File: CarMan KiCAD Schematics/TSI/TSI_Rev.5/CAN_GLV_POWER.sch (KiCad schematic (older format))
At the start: 40 parts, among them J30 J23, K2 G5LE-1-E, K3 SFS2-DC24V, K4 SFS2-DC24V, Q11 TN2130K1-G, U14 Bottom Left, U15 Top Left, U17 Top Right, U2 Bottom Right, U20 TLP293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

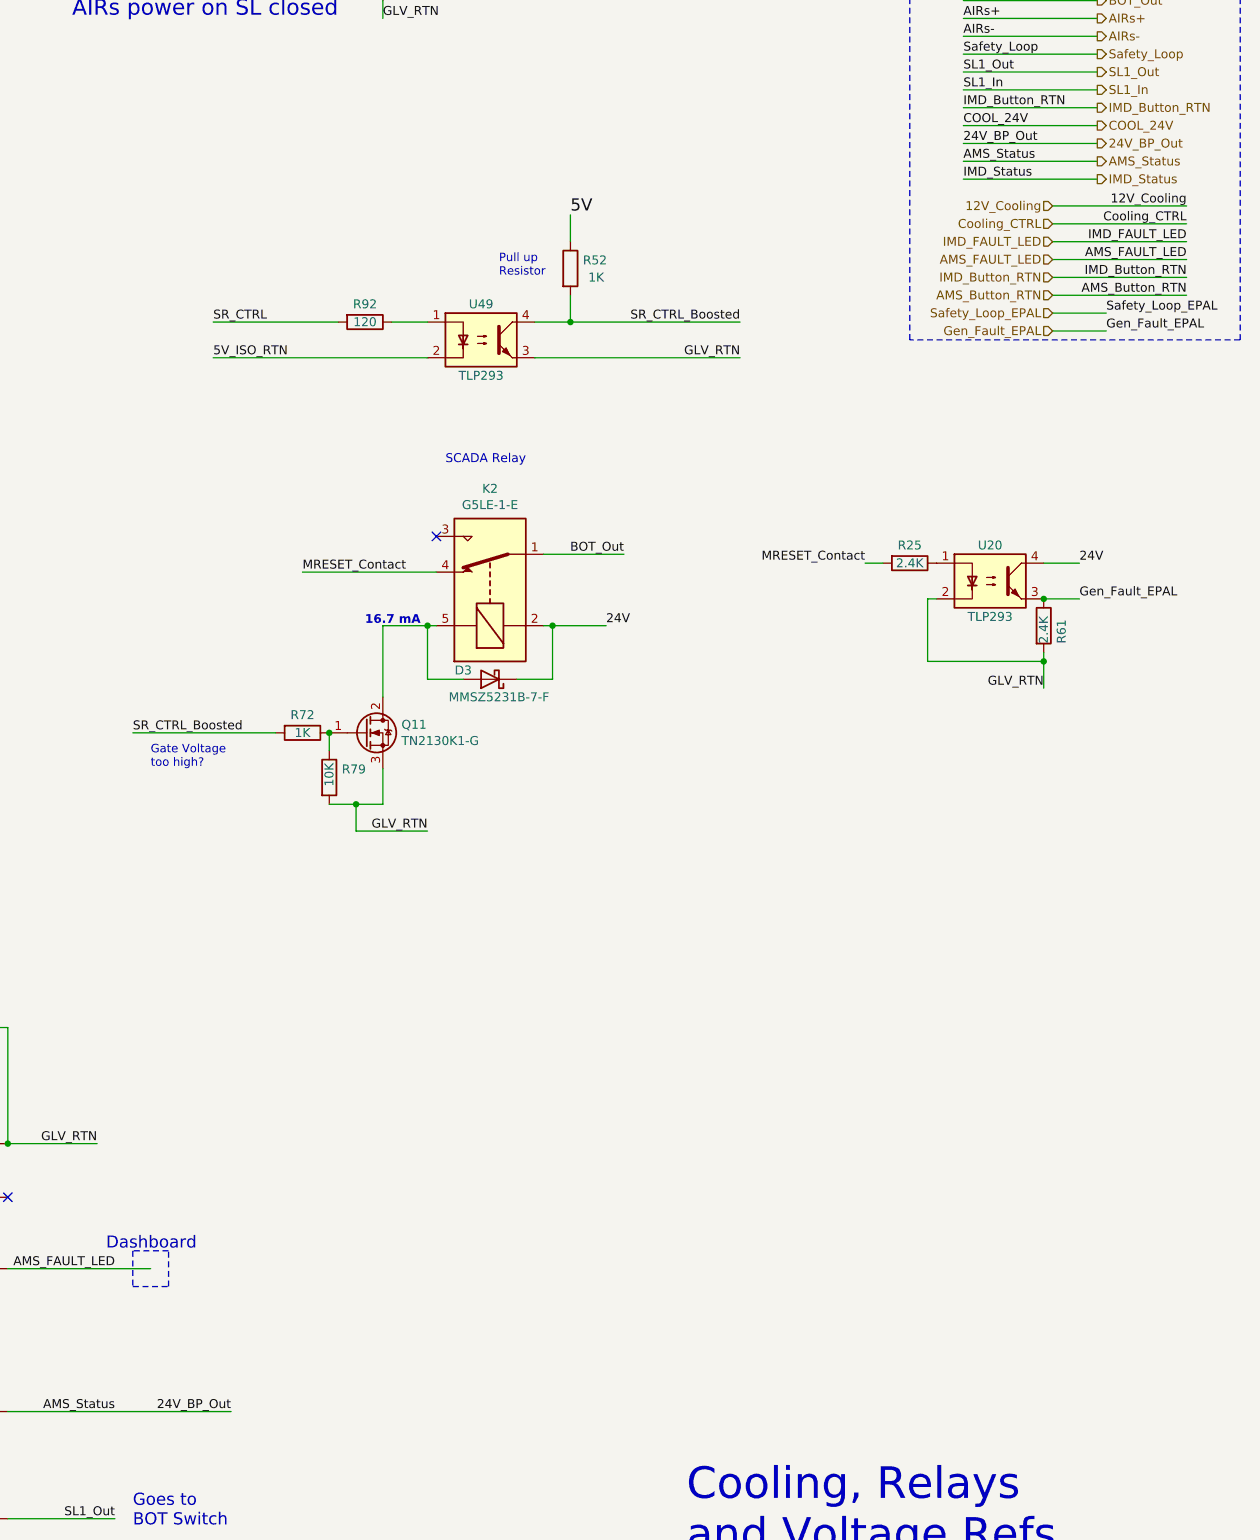
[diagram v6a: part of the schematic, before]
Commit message: -> Updated battery pack connections, matched order with that on the pacman board
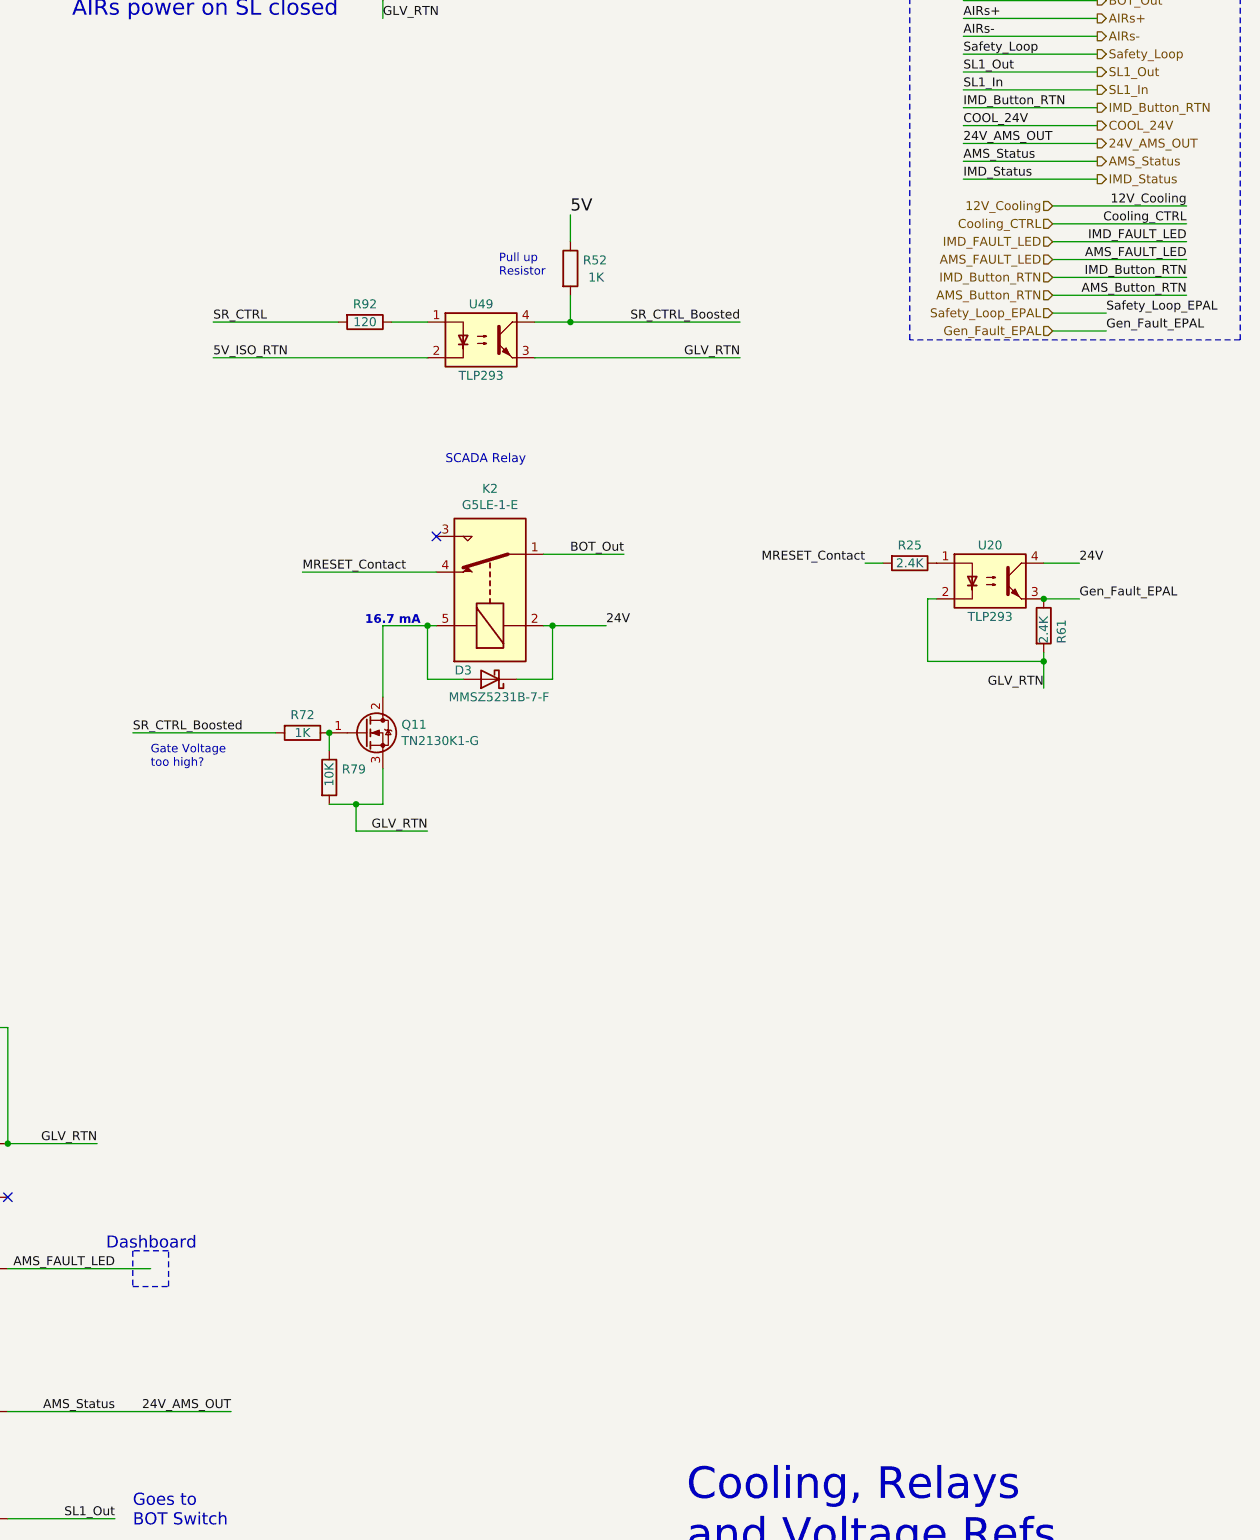
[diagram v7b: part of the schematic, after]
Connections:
- net labels added: 24V_AMS_OUT
- net labels removed: 24V_BP_Out
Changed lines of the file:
@@
 Text Label 6700 9200 0    50   ~ 0
 24V
-Text HLabel 15200 2600 2    50   Output ~ 0
-24V_BP_Out
 Wire Wire Line
 	14450 2600 15200 2600
 Text Label 14450 2600 0    50   ~ 0
-24V_BP_Out
+24V_AMS_OUT
 Text Label 10350 9700 2    50   ~ 0
-24V_BP_Out
+24V_AMS_OUT
 Wire Wire Line
 	9100 9700 10350 9700
@@
 Wire Wire Line
 	3650 4700 4350 4700
+Text HLabel 15200 2600 2    50   Output ~ 0
+24V_AMS_OUT
 $EndSCHEMATC

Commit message: Changed signal notation for J11
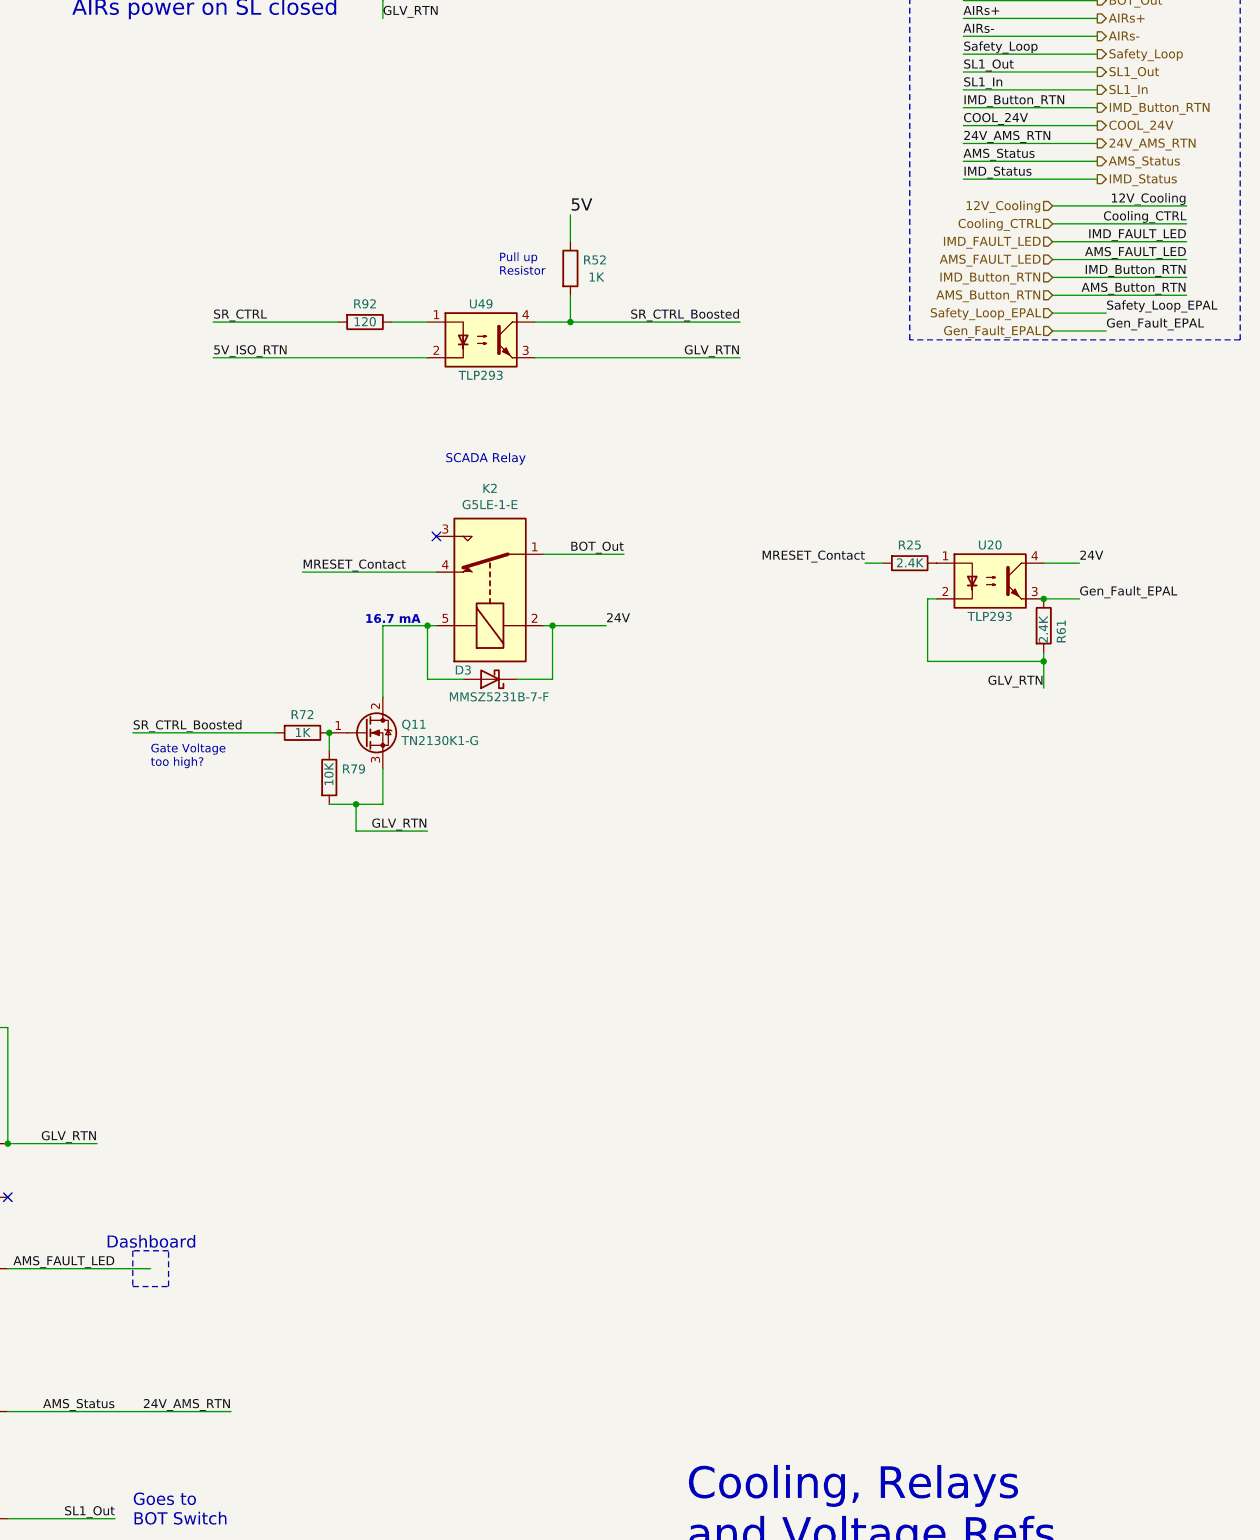
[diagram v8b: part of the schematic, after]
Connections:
- net labels added: 24V_AMS_RTN
- net labels removed: 24V_AMS_OUT
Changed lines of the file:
@@
 	14450 2600 15200 2600
 Text Label 14450 2600 0    50   ~ 0
-24V_AMS_OUT
+24V_AMS_RTN
 Text Label 10350 9700 2    50   ~ 0
-24V_AMS_OUT
+24V_AMS_RTN
 Wire Wire Line
 	9100 9700 10350 9700
@@
 	3650 4700 4350 4700
 Text HLabel 15200 2600 2    50   Output ~ 0
-24V_AMS_OUT
+24V_AMS_RTN
 $EndSCHEMATC
